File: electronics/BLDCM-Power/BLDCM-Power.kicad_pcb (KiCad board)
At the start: 4 copper layers, 32 x 32 mm, 60 parts, among them J1 501920-3001, J2 53048-0310, J3 505578-0460, J4 505578-0460, J5 FTSH-107-01-L-DV-K, J6 12402012E212A, U1 INA240A1PWR, U10 BAT54S, U11 BAT54S, U12 BAT54S, U2 LDLN030G33R, U3 TMC6300-LA, U4 INA240A1PWR, U5 TCAN1462, U6 INA240A1PWR, U7 BAT54S, U8 LDO40LPU50RY, U9 TPS2115ADRB

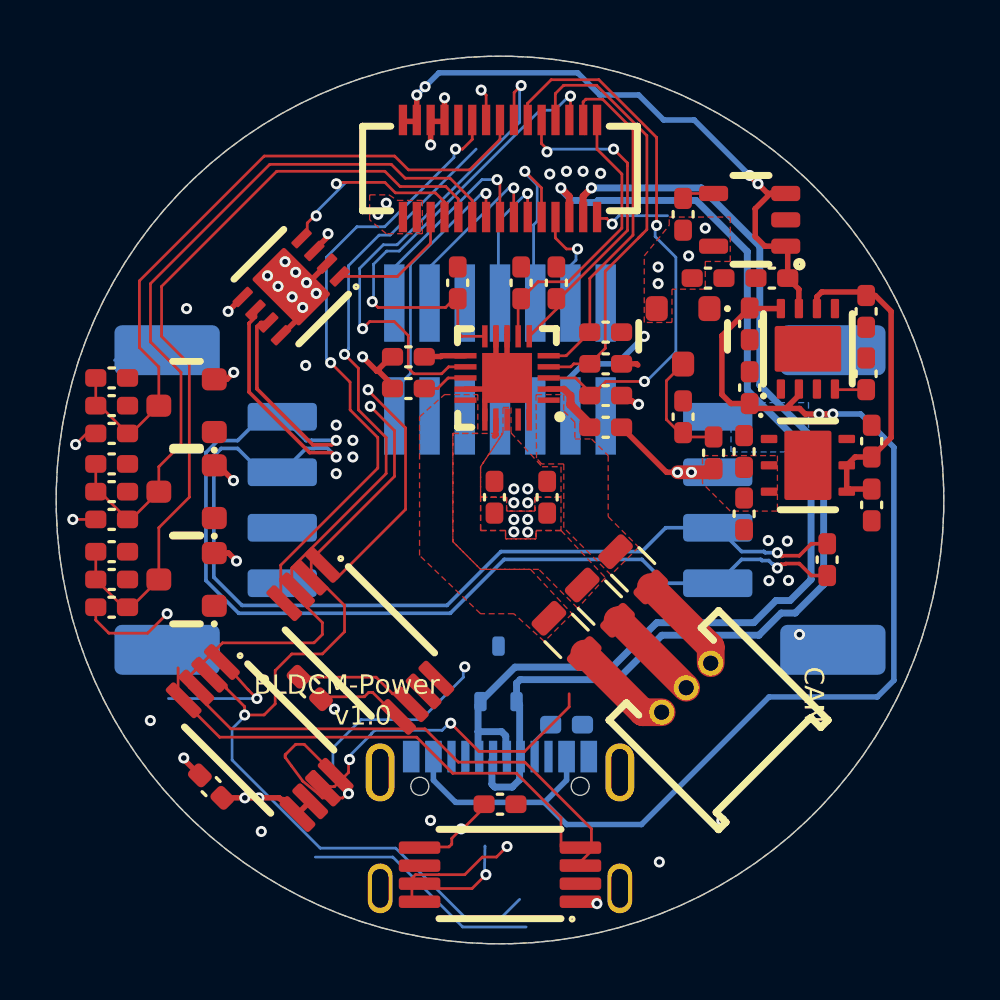
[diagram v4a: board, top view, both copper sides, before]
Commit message: Feat(pcb): Route volt/curr sense
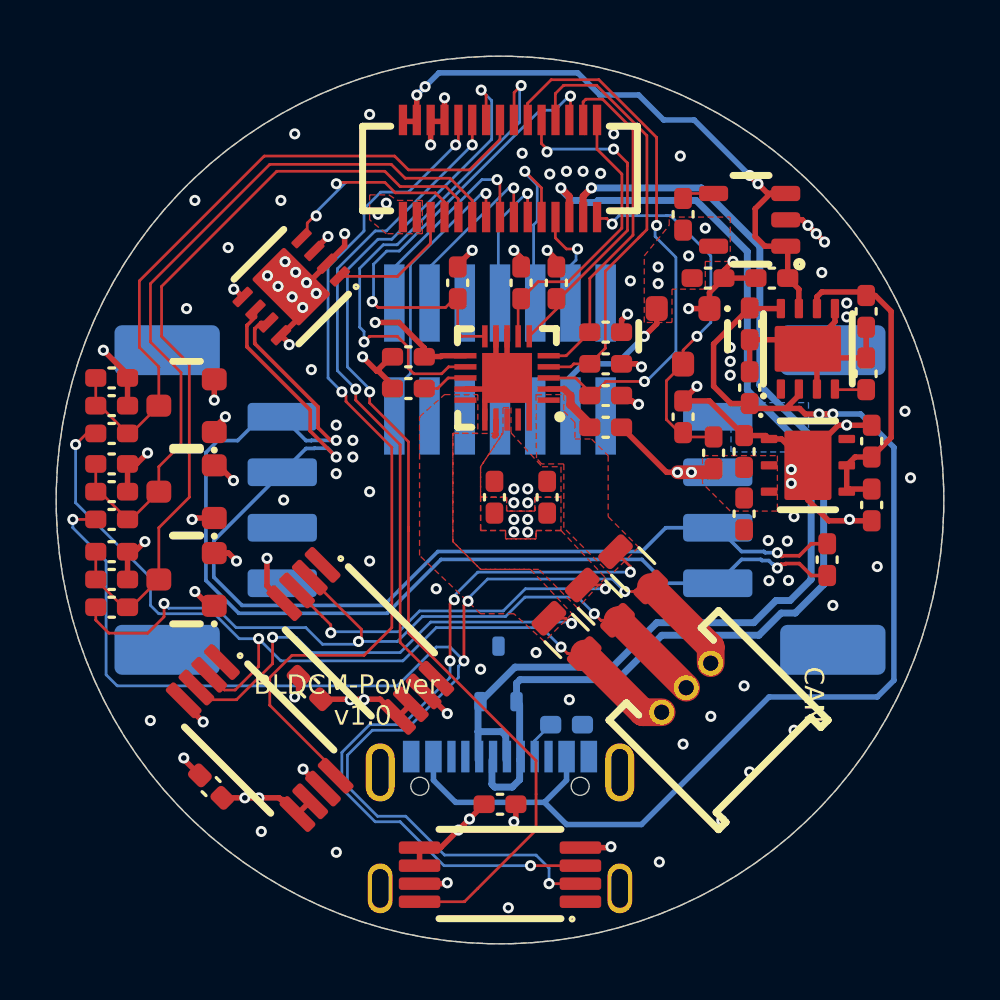
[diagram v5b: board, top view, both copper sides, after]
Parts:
- turned R10 to -90 degrees
- turned R5 to 180 degrees
- turned R6 to -90 degrees
- turned R7 to 180 degrees
- turned R8 to -90 degrees
- turned R9 to 180 degrees
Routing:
- net (no net): track 129.9 -> 0.00 mm
- net GND: track 21.6 -> 70.3 mm, vias 35 -> 100
- net /TMC.W.OUT: track 7.41 -> 50.4 mm, vias 2 -> 5
- net /INA.W: track 1.20 -> 38.7 mm, vias 3 -> 2
- net /INA.U: track 0.00 -> 31.5 mm, vias 0 -> 2
- net /INA.V: track 1.40 -> 23.8 mm
- net /TMC.V.OUT: track 7.00 -> 28.4 mm, vias 1 -> 3
- net /TMC.W.IN: track 5.68 -> 26.7 mm, vias 1 -> 4
- net /TMC.U.OUT: track 16.8 -> 32.2 mm
- net /TMC.V.IN: track 0.62 -> 14.1 mm, vias 0 -> 2
- net unconnected-(U6-NC-Pad1): track 8.65 -> 0.00 mm, vias 1 -> 0
- net /VOLT.SRC: track 7.02 -> 13.5 mm, vias 1 -> 2
- net 3.3V: track 20.0 -> 24.7 mm, vias 16 -> 19
- net /TMC.U.IN: track 12.8 -> 16.8 mm
- net /CAN.DN: track 41.2 -> 38.3 mm
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
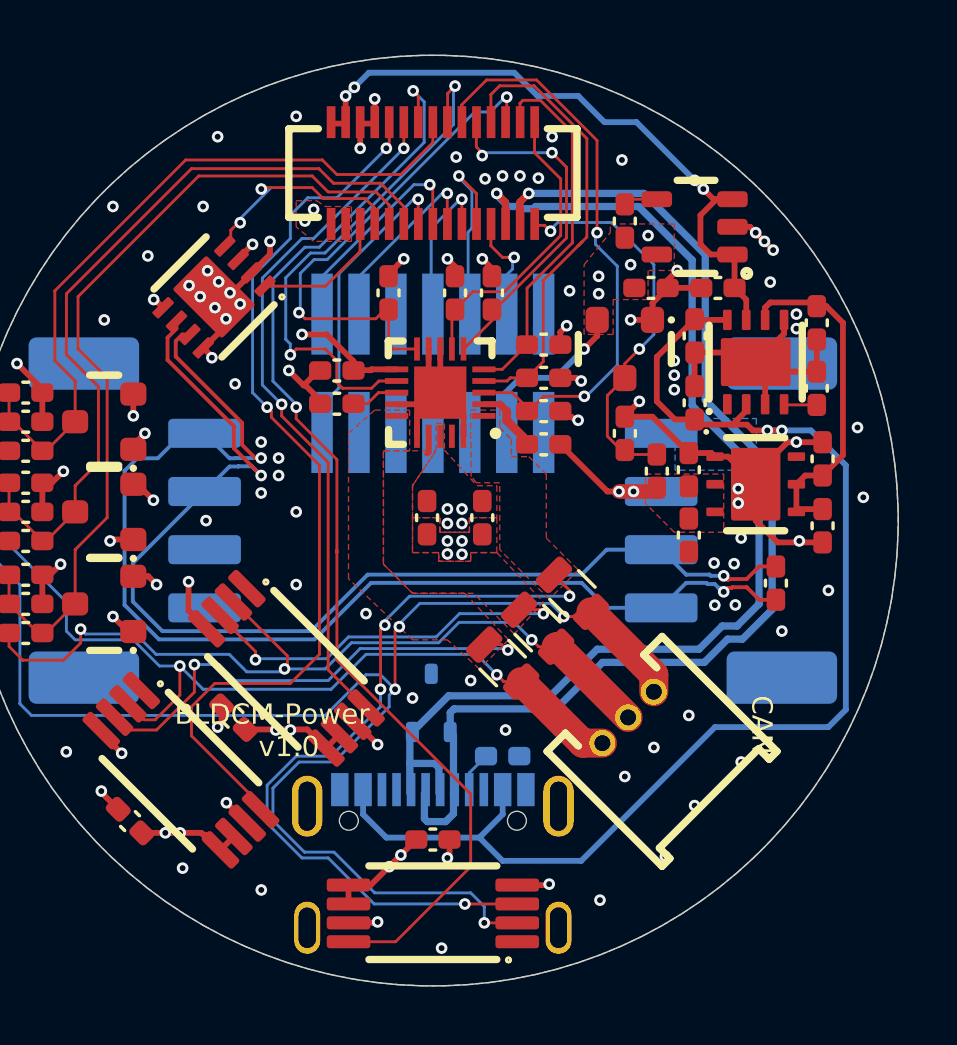
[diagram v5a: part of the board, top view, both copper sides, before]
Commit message: Fix(pcb): DRC errors
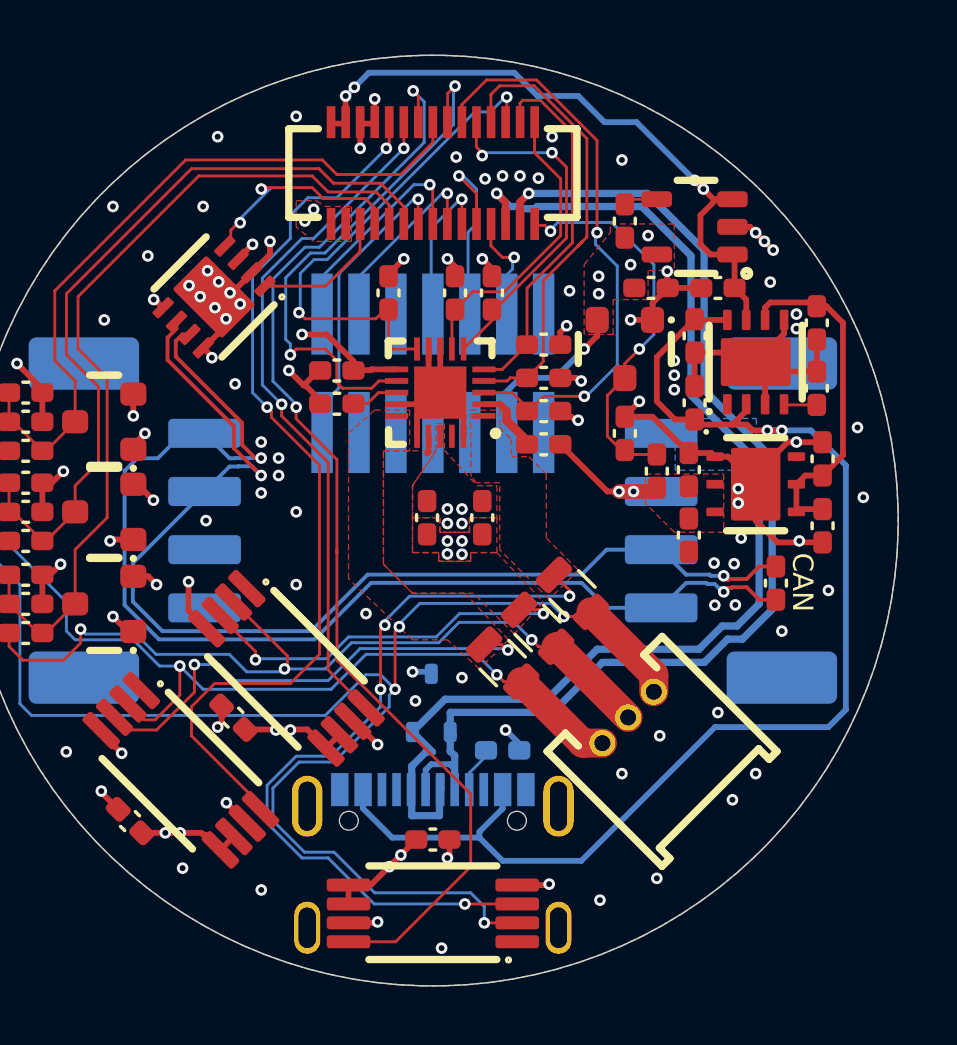
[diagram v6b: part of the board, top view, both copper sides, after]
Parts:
- moved R3 0.20 mm to (152.4, 107.9)
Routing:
- net /USB.DP: track 39.5 -> 41.9 mm
- net GND: track 70.3 -> 71.7 mm, vias 100 -> 101

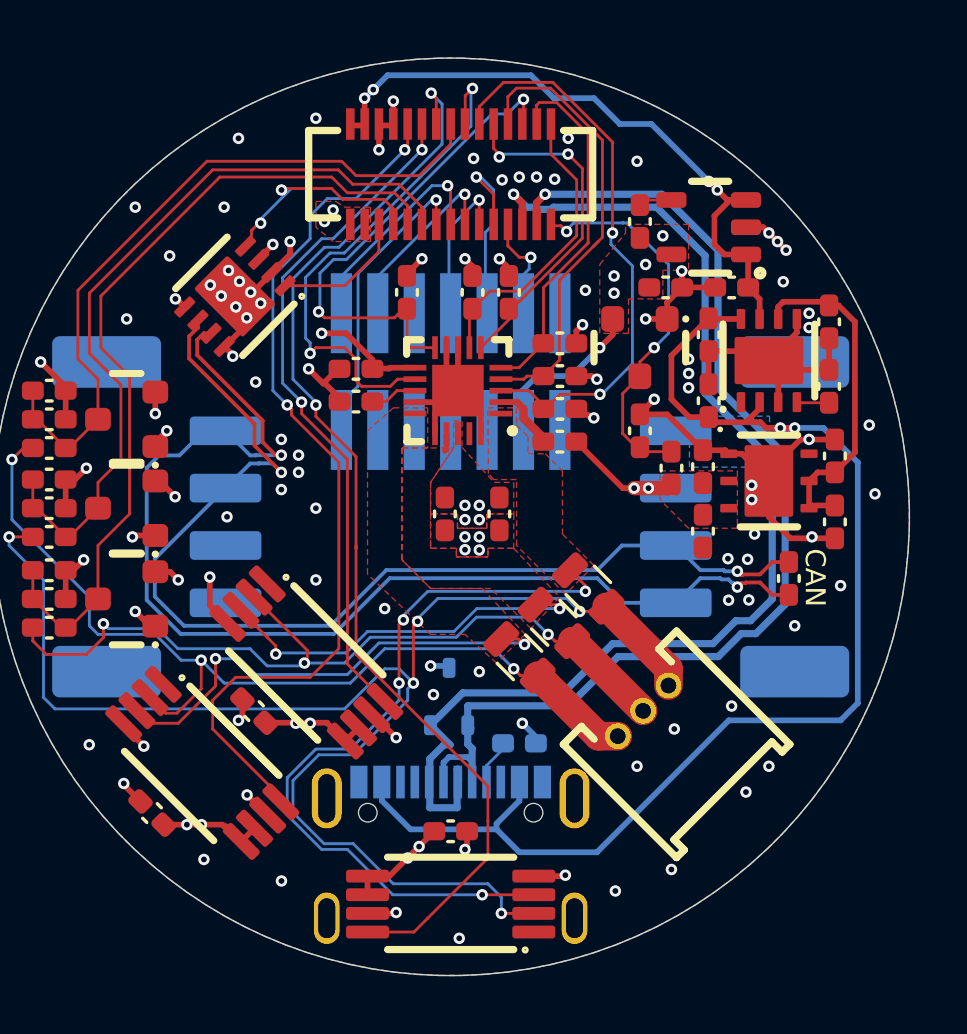
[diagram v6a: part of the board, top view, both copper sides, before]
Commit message: Refactor(pcb): Update footprints
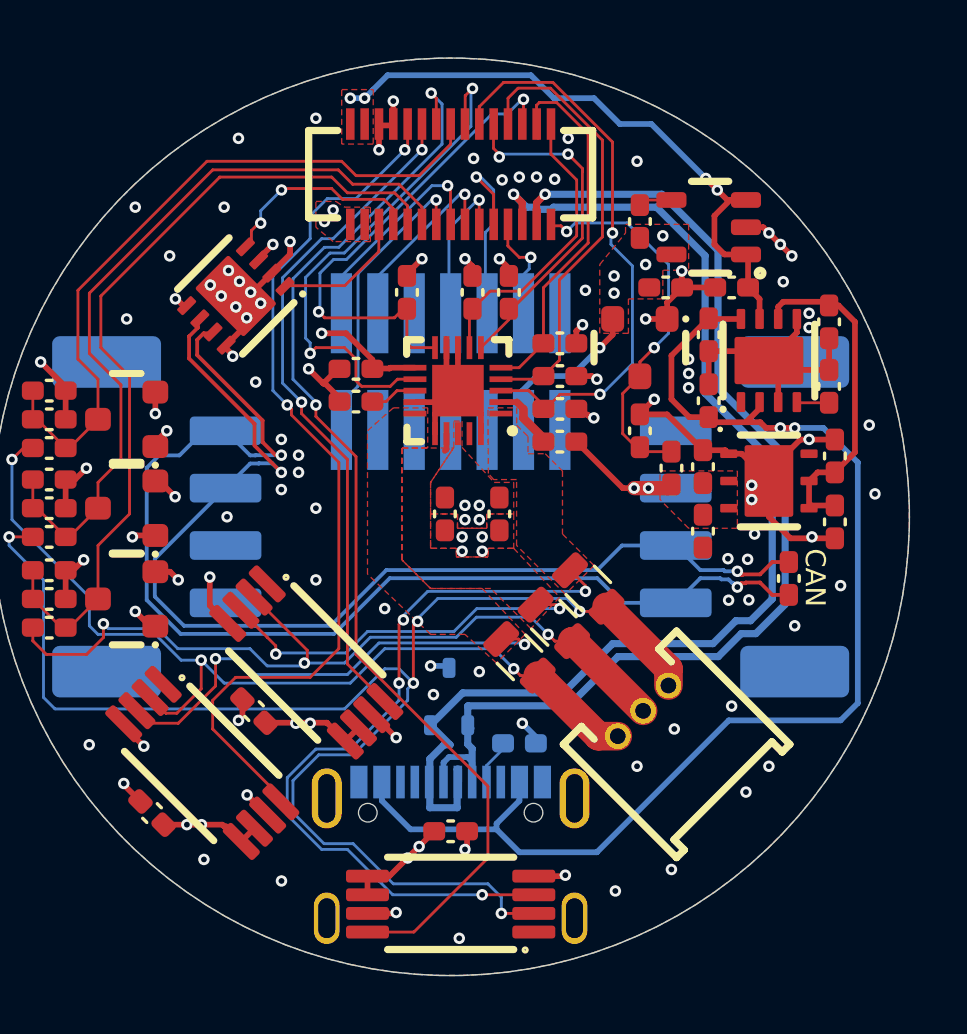
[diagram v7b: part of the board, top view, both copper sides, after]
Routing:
- net /TMC.VH: track 16.5 -> 15.8 mm
- net 5V: track 23.2 -> 22.5 mm
- added copper zone on F.Cu, net 5V
- removed copper zone on B.Cu, net VIN

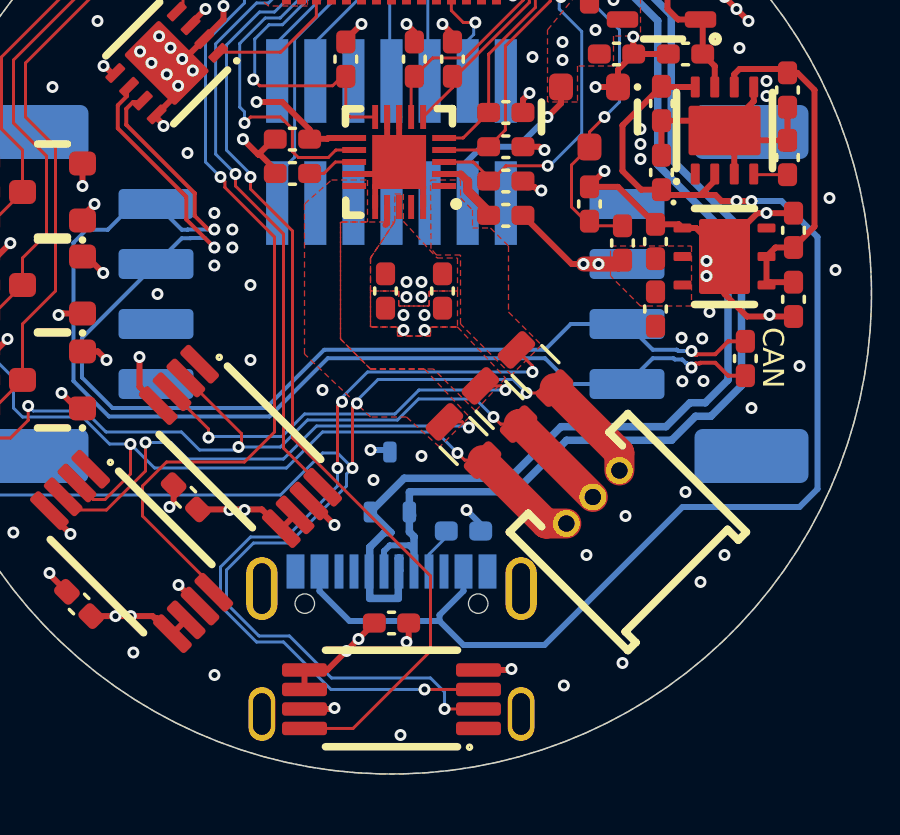
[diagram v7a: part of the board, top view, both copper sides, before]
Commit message: Feat(pcb): Replace USB with Molex USB
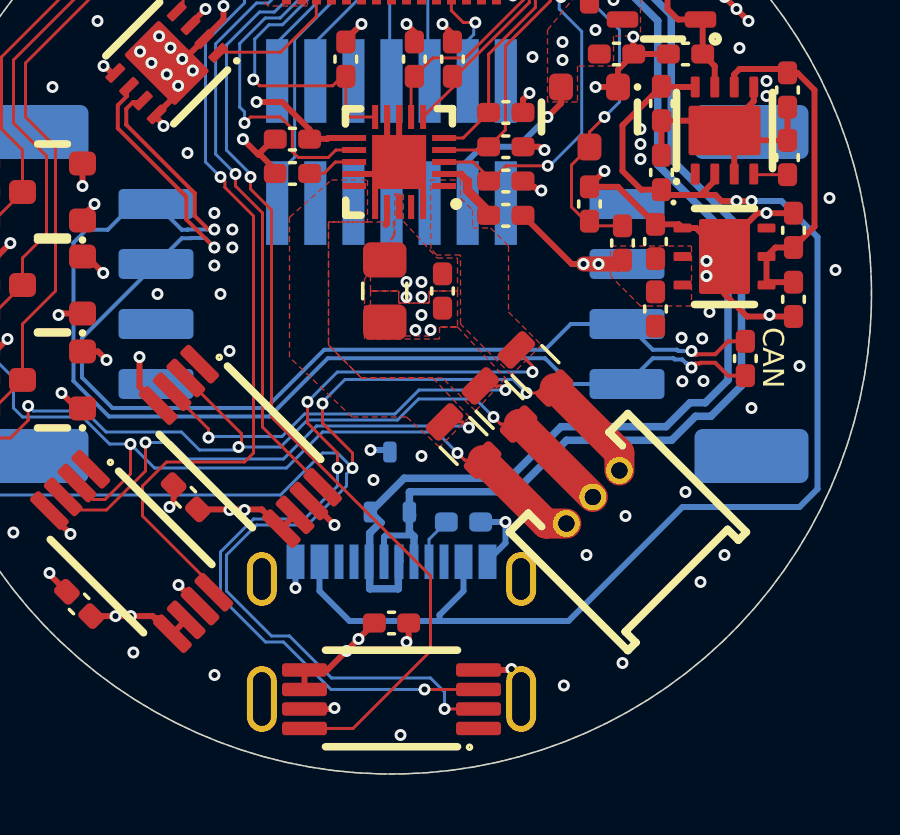
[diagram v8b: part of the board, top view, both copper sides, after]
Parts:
- C9: footprint BrenoCQ:C_0402 -> BrenoCQ:C_0805
- J6: value 12402012E212A -> 217179-0001; footprint BrenoCQ:12402012E212A -> BrenoCQ:217179-0001
- moved J6 0.50 mm to (150.0, 113.5)
- moved R3 0.30 mm to (152.4, 107.6)
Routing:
- net GND: track 72.0 -> 74.2 mm, vias 101 -> 100
- net /TMC.W.IN: track 26.7 -> 28.3 mm
- net /TMC.W.OUT: track 50.4 -> 51.9 mm
- net /USB.DP: track 41.9 -> 41.2 mm
- net VBUS: track 43.6 -> 42.9 mm
- net /INA.U: track 31.5 -> 30.9 mm
